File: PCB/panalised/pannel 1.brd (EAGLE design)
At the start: 84 x 82.7 mm, 84 parts, among them IC1 LM386M-1, IC5 LM321MF, J1 AVR_SPI_PRG_6PTH, J2 POWERPOLE_POWER25A_HORIZONTAL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, J3 POWER_JACKPTH, Q1 MMBT3904, Q2 MMBT3904, Q3 MMBT3904, Q4 2.5A/30V/105mΩ, Q5 MMBT3904, T1 MMBTA42, U1 ATMEGA328P_TQFP

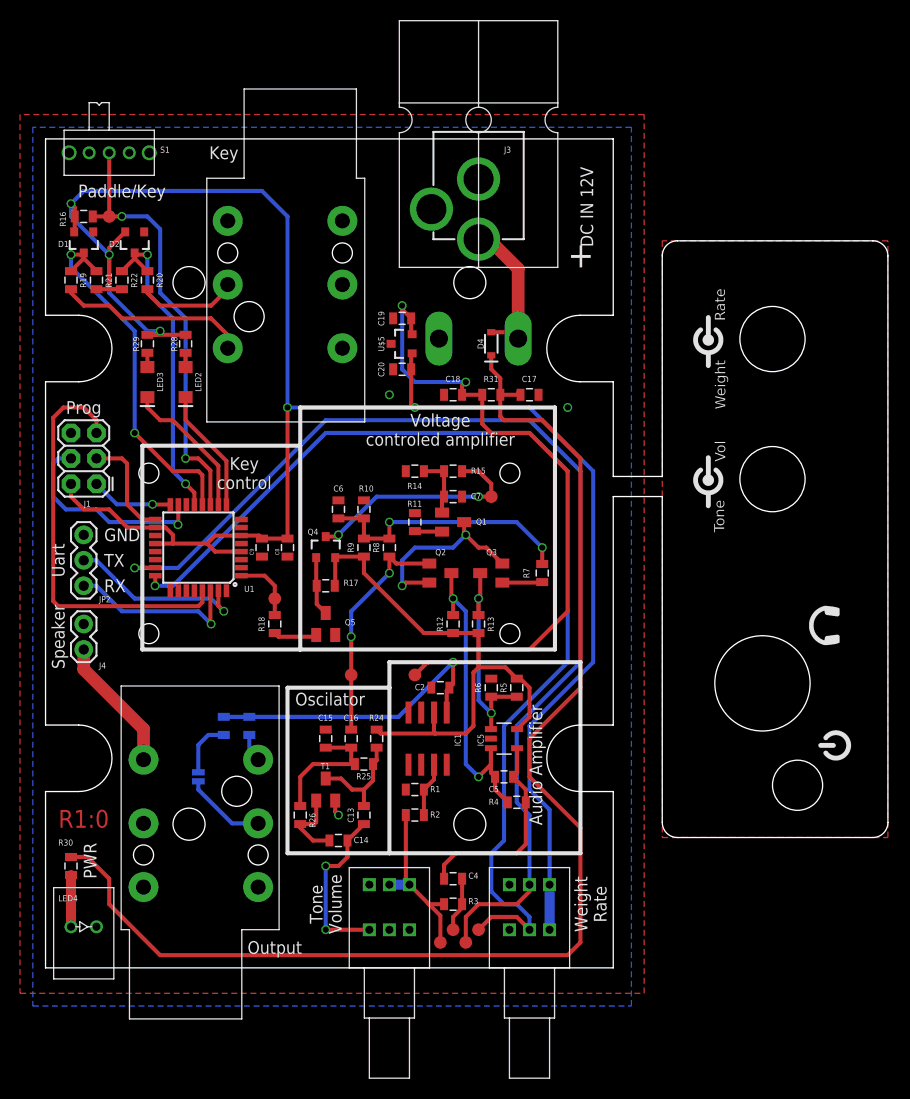
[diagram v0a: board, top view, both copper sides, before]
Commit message: Merged new board and front panel onto single panel for manufacture
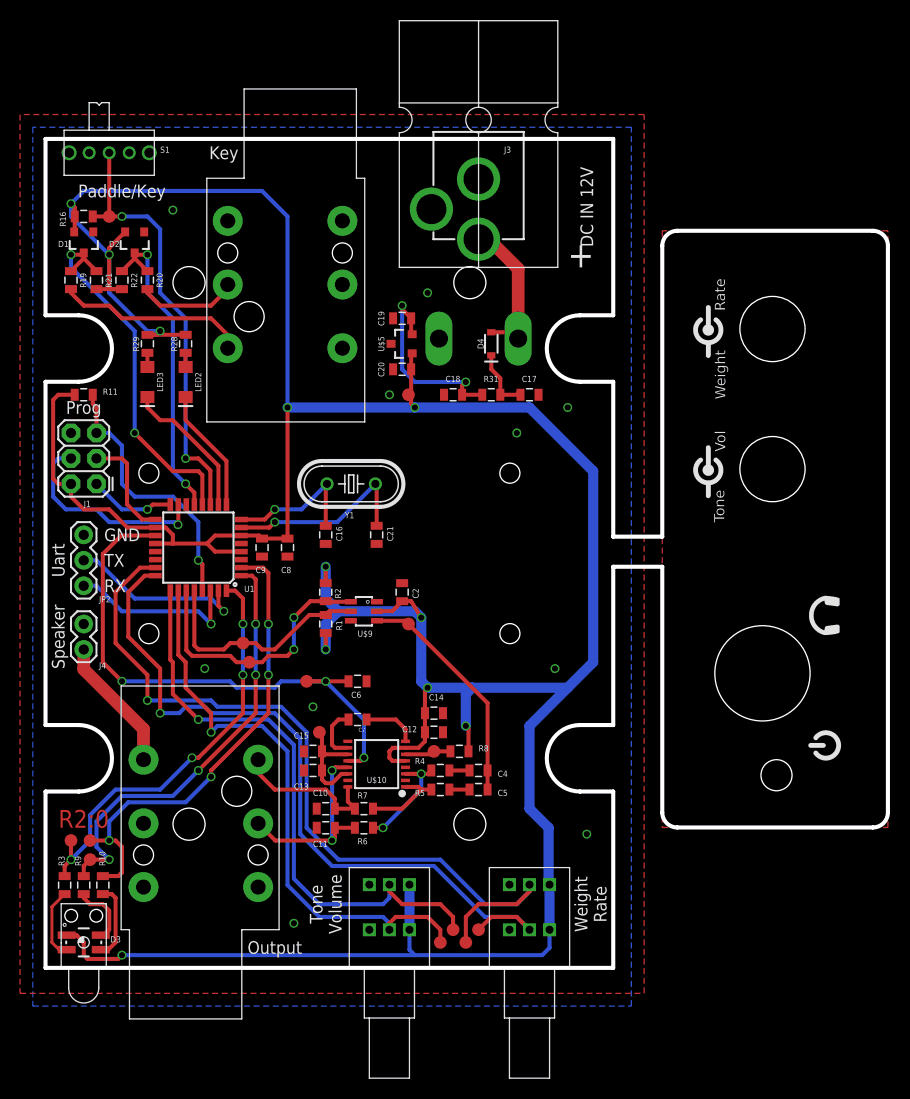
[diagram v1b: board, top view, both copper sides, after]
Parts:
- removed C1, C3: 100u, SparkFun:0805
- removed IC1: LM386M-1, linear:SO08
- removed IC5: LM321MF, linear:SOT23-5
- removed LED4: LED-902118128, morseSounder:MULTICOMP-2118128
- removed Q1, Q2, Q3, Q5: MMBT3904, transistor:SOT23-BEC
- removed Q4: 2.5A/30V/105mΩ, SparkFun-DiscreteSemi:SOT23-3
- removed R12, R13, R14, R15, R30: 22K, SparkFun:0805
- removed R17, R18: 10K, SparkFun:0805
- removed R24: 4.7K, SparkFun:0805
- removed R25, R26: 18K, SparkFun:0805
- removed SJ1: SOLDERJUMPERNO, SparkFun:SJ_2S-NO
- removed T1: MMBTA42, SparkFun:SOT23
- added C10, C11: 1n, SparkFun:0805
- added C12: 1u, SparkFun:0805
- added C21: 22p, SparkFun:0805
- added D3: RGB, morseSounder:P-LCC-4-3
- added TP10, TP11, TP12, TP13, TP14, TP15: TEST-POINT3X5, SparkFun-Connectors:PAD.03X.05
- added U$10: MAX13331, morseSounder:SSOP16
- added U$8: SLP3SLP3, morseSounder:SLP-3
- added U$9: DAC_MCP4725SOT, SparkFun:SOT23-6
- added Y1: (no value), SparkFun:HC49U-V
- C13: value 0.018u -> 1u
- C14: value 0.018u -> 100n
- C15: value 0.047u -> 100n
- C16: value 0.047u -> 22p
- C2: value 200n -> 1u
- C4: value 100n -> 330n
- C5: value 10n -> 330n
- C6: value 100u -> 1n
- C7: value 100n -> 1u
- R1: value 1K -> 10K
- R10, R3, R9: value 10K -> 330
- R11: value 22K -> 10K
- R2: value 15K -> 10K
- R4, R5: value 10K -> 30K
- R6: value 10K -> 45K
- R7: value 330 -> 45K
- R8: value 330 -> 10K
- moved R10 45.6 mm to (5.71, 8.26), turned to 270 degrees
- moved R9 43.7 mm to (3.81, 8.26), turned to 270 degrees
- moved R3 38.8 mm to (1.91, 8.26), turned to 270 degrees
- moved R11 35.4 mm to (3.81, 57.1), turned to 0 degrees
- moved TP8 31.9 mm to (36.2, 34.3)
- moved R7 29.5 mm to (31.8, 15.9), turned to 0 degrees
- moved TP7 29.2 mm to (20.3, 30.5)
- moved TP4 25.7 mm to (40.6, 3.81)
- moved C7 24.2 mm to (31.1, 24.8)
- moved R2 23.9 mm to (27.9, 37.5), turned to 90 degrees
- moved R8 21.5 mm to (41.3, 21.6), turned to 0 degrees
- moved C16 20.5 mm to (27.9, 43.2)
- moved R6 18.9 mm to (31.8, 14.0), turned to 0 degrees
- moved R1 18.8 mm to (27.9, 34.3), turned to 270 degrees
- moved C6 17.3 mm to (31.1, 28.6), turned to 0 degrees
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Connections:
- removed net AUDIO_OUT: C1.1, C2.1, C3.1, IC1.5, TP4.P$1
- removed net AUDIO_PRE_AMP: C4.2, R3.1, TP5.P$1
- removed net AVR_KEY_OUT: R18.1, TP9.P$1, U1.1
- removed net KEY_IN: Q4.3, R15.2, TP7.P$1
- removed net N$11: Q3.B, R7.2
- removed net N$12: C6.2, R10.1, R7.1, R8.2, R9.2
- removed net N$13: Q1.E, R11.2
- removed net N$14: SJ1.2, U$2.P$5
- removed net N$24: C14.1, R26.1, T1.1
- removed net N$25: C15.1, C16.1, R25.1, R26.2
- removed net N$26: C13.1, C14.2, U$3.F1
- removed net N$36: LED4.P$1, R30.1
- removed net N$9: C7.2, Q1.B, R14.2, R15.1
- new net ADC_MAX13331_DIAG: C6.1, TP12.P$1, U$10.12, U1.19
- new net ADC_TONE: TP5.P$1, U$3.F2, U1.26
- new net ADC_VOLUME: TP4.P$1, U$3.R2, U1.25
- new net LED_FRONT_BLU: R9.1, TP14.P$1, U1.1
- new net LED_FRONT_GRN: R10.1, TP15.P$1, U1.2
- new net LED_FRONT_RED: R3.1, TP13.P$1, U1.32
- new net N$19: D3.2, R3.2
- new net N$20: R8.1, TP11.P$1, U$10.6
- new net OUT_L: C10.1, R7.1, U$10.16, U$2.P$6
- new net OUT_R: C11.1, R6.1, U$10.13, U$2.P$5
- new net SCL: R1.1, TP6.P$1, U$9.5, U1.28
- new net SDA: R2.1, TP7.P$1, U$9.6, U1.27
- net +12V: no longer IC1.6, IC5.5, Q4.2, R12.1, R13.1, R17.2, R24.1, R5.1, R9.1
- net AVR_RESET: now also R11.2
- net AVR_VCC: now also C12.1, C14.1, C2.2, D3.1, R1.2, R11.1, R2.2, R8.2, TP10.P$1, U$10.5, U$10.7, U$3.F3, U$3.R3, U$9.2
- net GND: now also C10.2, C11.2, C12.2, C13.2, C14.2, C16.1, C2.1, C21.1, C6.2, U$10.15, U$10.2, U$10.4, U$10.9, U$3.F1, U$9.1, U$9.4; no longer C2.2, C6.1, C7.1, IC1.2, IC1.4, IC5.2, LED4.P$2, Q5.E, R1.1, R10.2, R11.1, R14.1, R6.2, T1.2, U$3.F2
- net N$1: now also C21.2, U1.7, Y1.2; no longer C3.2, U$2.P$6
- net N$15: now also D3.4, R9.2; no longer R2.2, R3.2, TP8.P$1, U$3.R2, U$3.R3
- net N$16: now also C7.1, U$10.8; no longer Q5.B, R18.2
- net N$17: now also C7.2, U$10.10; no longer Q4.1, Q5.C, R17.1
- net N$2: now also C16.2, U1.8, Y1.1; no longer C1.2, SJ1.1
- net N$23: now also C13.1, C15.1, TP9.P$1, U$10.11, U$10.14; no longer C13.2, R24.2, R25.2, T1.3
- net N$3: now also D3.3, R10.2; no longer IC1.3, R1.2, R2.1
- net N$4: no longer R30.2
- net N$5: now also C4.2, R4.2; no longer C4.1, C5.2, IC5.4, R4.1
- net N$6: now also C5.2, R5.2; no longer C5.1, IC5.3, Q2.C, R12.2, R4.2
- net N$7: now also R4.1, R6.2, U$10.3; no longer IC5.1, Q3.C, R13.2, R5.2, R6.1
- net N$8: now also R5.1, R7.2, U$10.1; no longer Q1.C, Q2.E, Q3.E
- net TONE_OUT: now also C4.1, C5.1, TP8.P$1, U$9.3; no longer C16.2, Q2.B, R8.1, TP6.P$1
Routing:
- net AVR_VCC: track 209.9 -> 348.4 mm, vias 5 -> 11
- net N$4: track 127.9 -> 6.64 mm
- net +12V: track 111.3 -> 19.9 mm
- net ADC_VOLUME: track 0.00 -> 59.4 mm, vias 0 -> 1
- net ADC_TONE: track 0.00 -> 57.9 mm, vias 0 -> 1
- net ADC_MAX13331_DIAG: track 0.00 -> 55.4 mm, vias 0 -> 3
- net LED_FRONT_GRN: track 0.00 -> 47.5 mm, vias 0 -> 4
- net LED_FRONT_BLU: track 0.00 -> 43.4 mm, vias 0 -> 4
- net LED_FRONT_RED: track 0.00 -> 41.9 mm, vias 0 -> 4
- net AUDIO_OUT: track 34.7 -> 0.00 mm, vias 1 -> 0
- net ADC_RATE: track 107.4 -> 74.8 mm
- net N$6: track 32.5 -> 2.01 mm, vias 2 -> 0
- net ADC_WEIGHT: track 109.7 -> 81.0 mm
- net SDA: track 0.00 -> 27.2 mm, vias 0 -> 2
- net N$12: track 26.7 -> 0.00 mm, vias 2 -> 0
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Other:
- outline, holes or cut-outs redrawn
- board text added: "R2:0"
- board text removed: "Audio Amplifier"
- board text removed: "Key control"
- board text removed: "Oscilator"
- board text removed: "PWR"
- board text removed: "R1:0"
- board text removed: "Voltage controled amplifier"

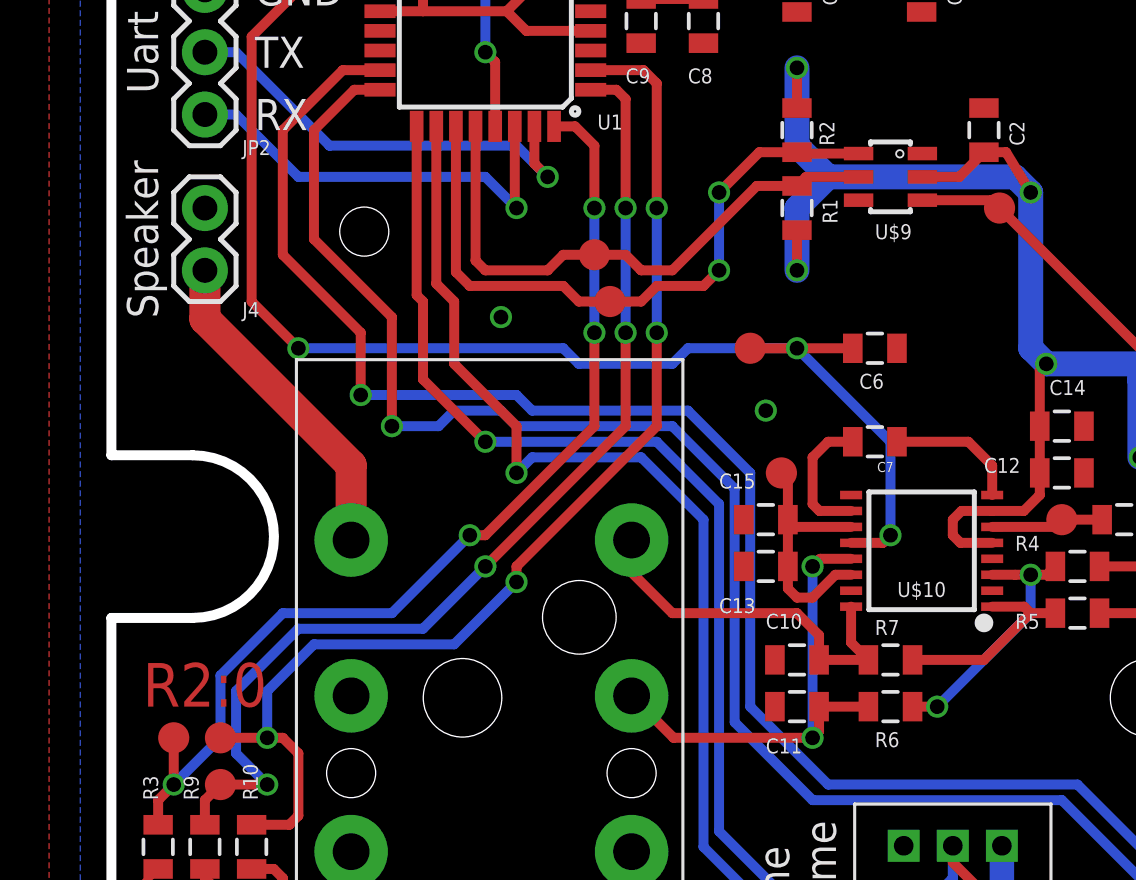
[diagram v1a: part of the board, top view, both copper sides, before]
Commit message: bumped version number on boards and updated panel 1 with new design
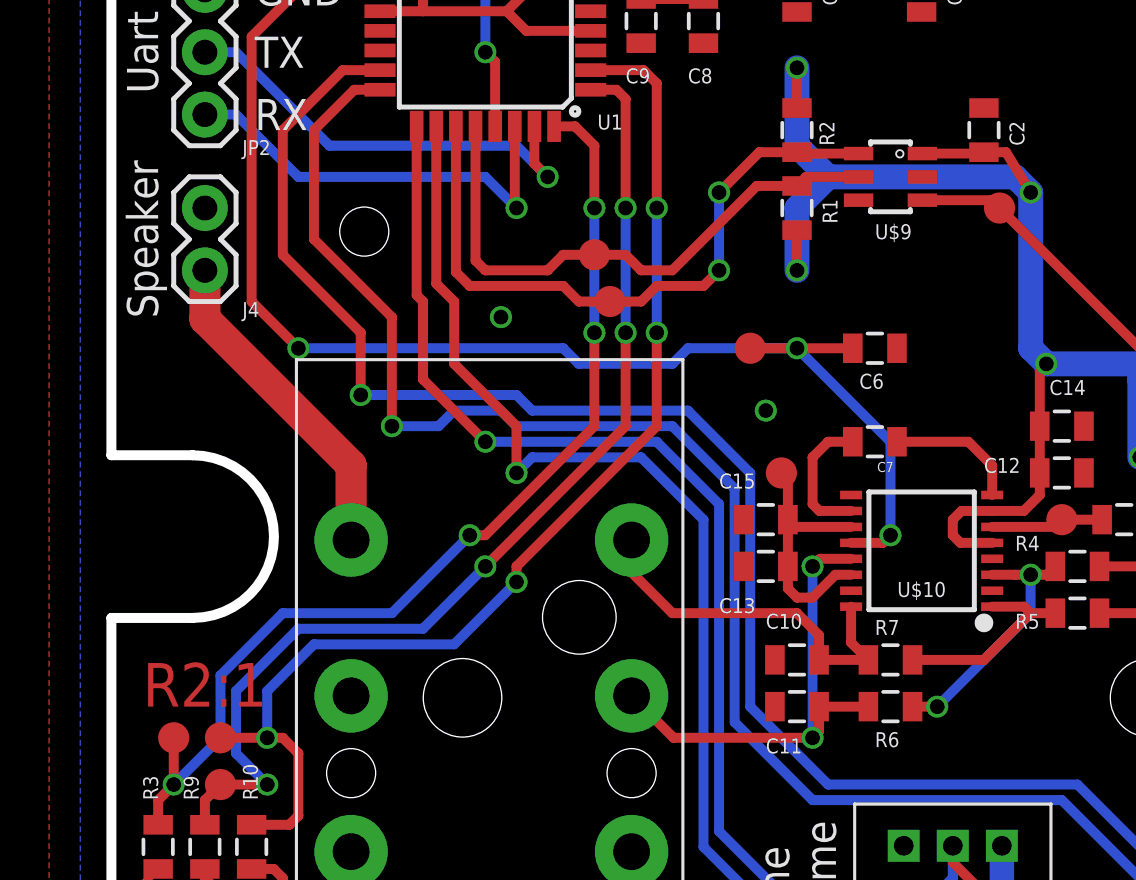
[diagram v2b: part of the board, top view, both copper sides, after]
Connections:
- net AVR_VCC: now also U$9.1; no longer U$9.2
- net GND: now also U$9.2; no longer U$9.1
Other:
- board text added: "R2:1"
- board text removed: "R2:0"
